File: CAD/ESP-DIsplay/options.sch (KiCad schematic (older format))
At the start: 0 parts

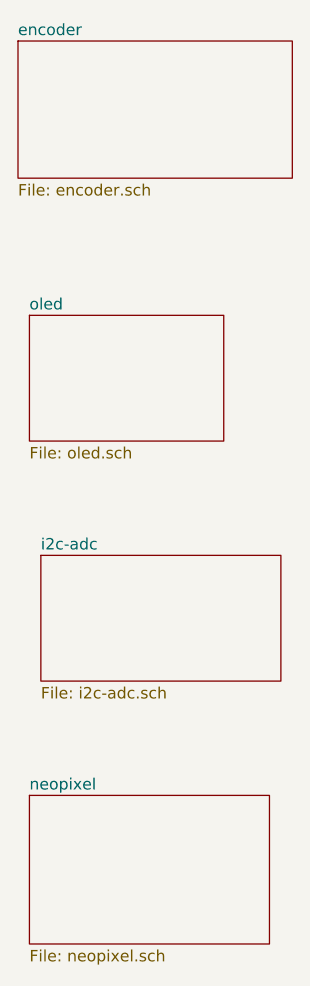
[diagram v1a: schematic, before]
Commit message: ESP Display v1
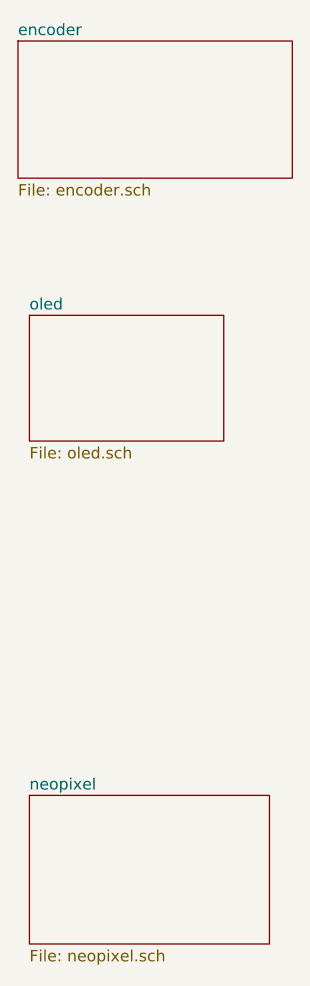
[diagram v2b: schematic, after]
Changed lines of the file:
@@
 $Descr A4 11693 8268
 encoding utf-8
-Sheet 4 9
+Sheet 4 8
 Title ""
 Date ""
@@
 F1 "neopixel.sch" 50
 $EndSheet
-$Sheet
-S 5000 4000 1050 550
-U 6035E9A5
-F0 "i2c-adc" 50
-F1 "i2c-adc.sch" 50
-$EndSheet
 $EndSCHEMATC
